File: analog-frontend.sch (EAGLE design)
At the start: 69 parts, among them IC1 TPS63031, IC2 ADG731, IC3 TM4C123G, IC4 INA332, IC5 NRF24L01SMD, IC6 OPA2320, Y1 CRYSTAL3X2, Y2 CRYSTAL3X2

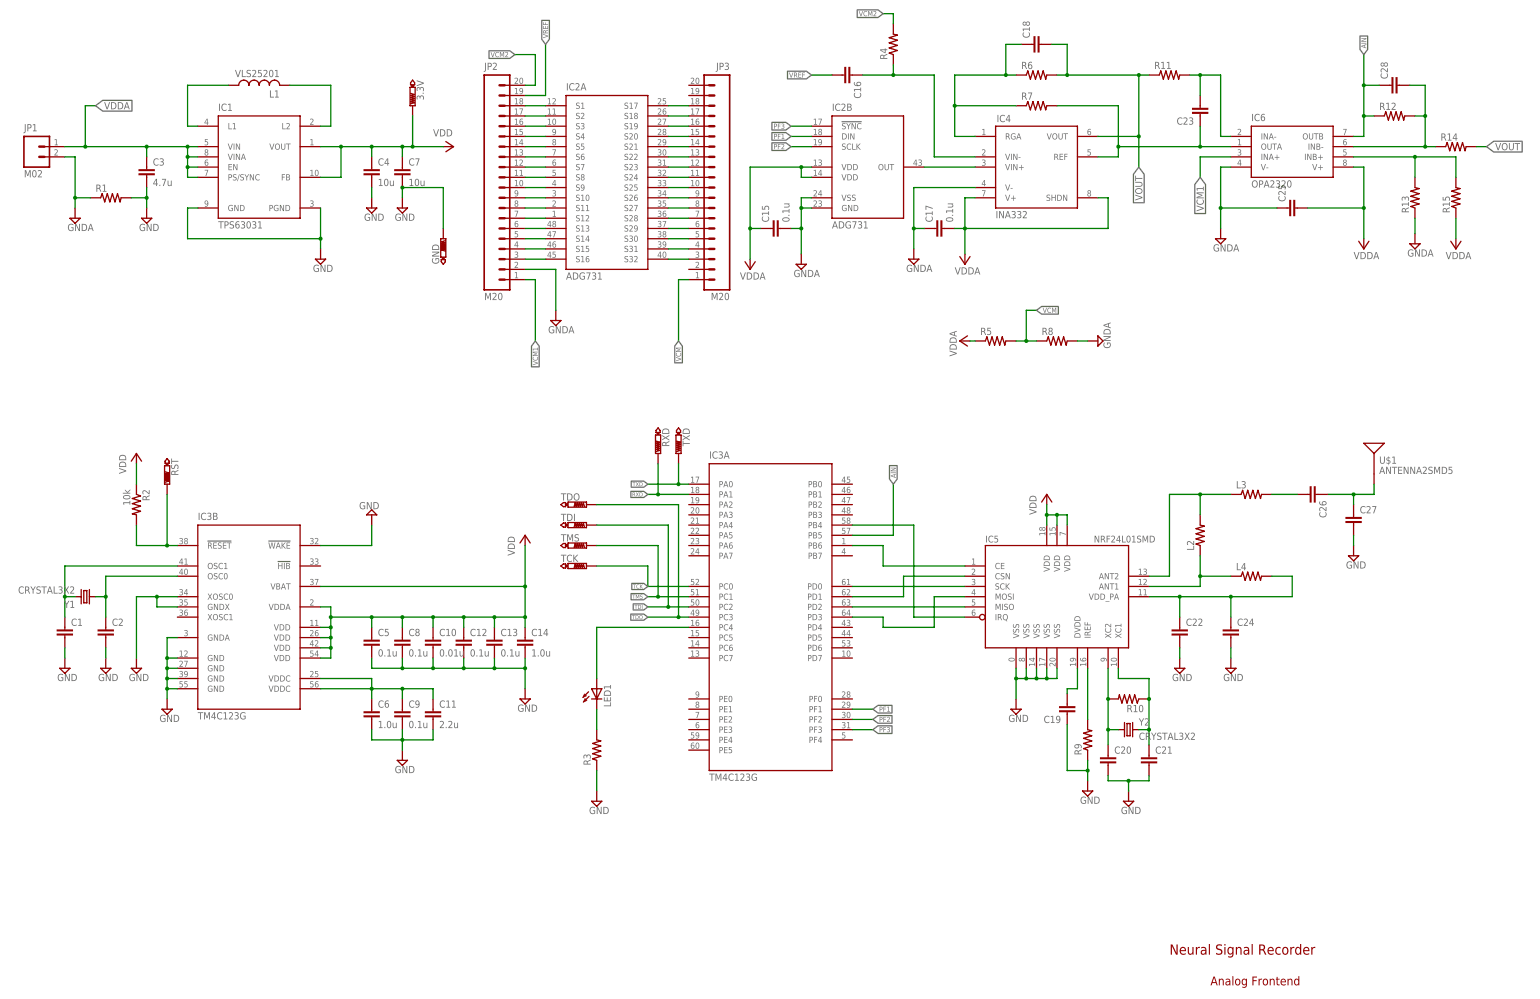
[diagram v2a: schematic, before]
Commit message: fixed component values
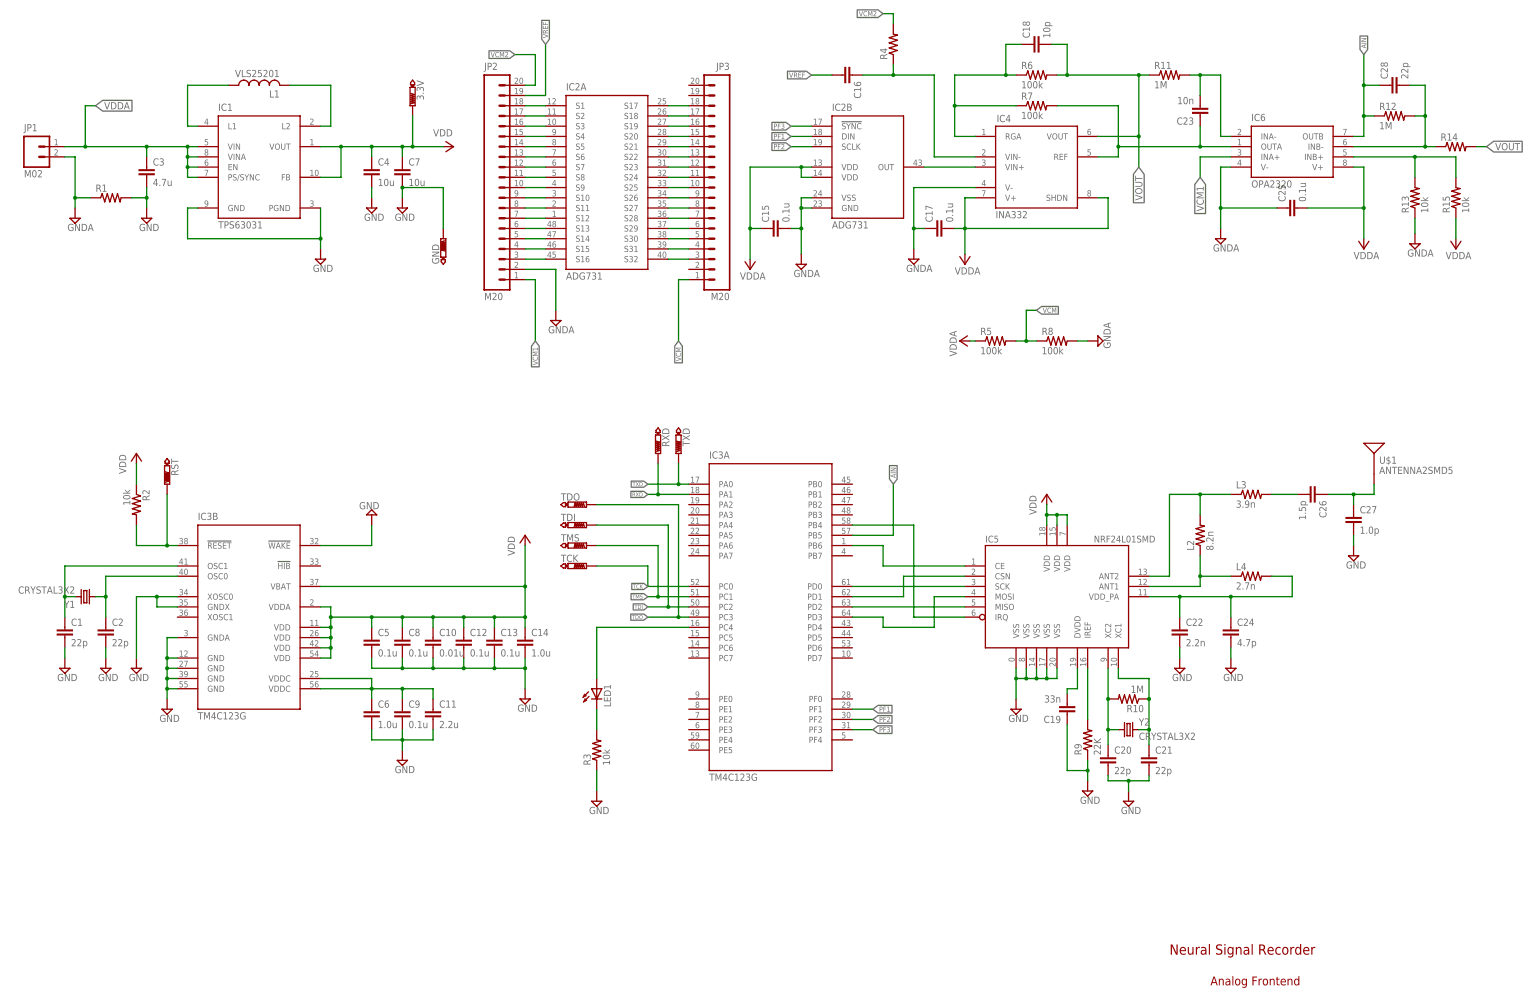
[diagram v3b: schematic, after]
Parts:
- C1, C2, C20, C21, C28: value (none) -> 22p
- C18: value (none) -> 10p
- C19: value (none) -> 33n
- C22: value (none) -> 2.2n
- C23: value (none) -> 10n
- C24: value (none) -> 4.7p
- C25: value (none) -> 0.1u
- C26: value (none) -> 1.5p
- C27: value (none) -> 1.0p
- L2: value (none) -> 8.2n
- L3: value (none) -> 3.9n
- L4: value (none) -> 2.7n
- R10, R11, R12: value (none) -> 1M
- R13, R15, R3: value (none) -> 10k
- R5, R6, R7, R8: value (none) -> 100k
- R9: value (none) -> 22K
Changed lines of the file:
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@@
 <part name="IC6" library="mor307" deviceset="OPA2320" device=""/>
 <part name="IC5" library="SparkFun-RF" deviceset="NRF24L01" device="SMD"/>
-<part name="R7" library="rcl" deviceset="R-US_" device="R0402"/>
-<part name="C18" library="rcl" deviceset="C-EU" device="C0402"/>
-<part name="R6" library="rcl" deviceset="R-US_" device="R0402"/>
-<part name="R11" library="rcl" deviceset="R-US_" device="R0402"/>
-<part name="C23" library="rcl" deviceset="C-EU" device="C0402"/>
+<part name="R7" library="rcl" deviceset="R-US_" device="R0402" value="100k"/>
+<part name="C18" library="rcl" deviceset="C-EU" device="C0402" value="10p"/>
+<part name="R6" library="rcl" deviceset="R-US_" device="R0402" value="100k"/>
+<part name="R11" library="rcl" deviceset="R-US_" device="R0402" value="1M"/>
+<part name="C23" library="rcl" deviceset="C-EU" device="C0402" value="10n"/>
 <part name="C17" library="rcl" deviceset="C-EU" device="C0402" value="0.1u"/>
 <part name="SUPPLY5" library="supply2" deviceset="GND" device="" value="GNDA"/>
-<part name="C25" library="rcl" deviceset="C-EU" device="C0402"/>
+<part name="C25" library="rcl" deviceset="C-EU" device="C0402" value="0.1u"/>
 <part name="SUPPLY6" library="supply2" deviceset="GND" device="" value="GNDA"/>
 <part name="R14" library="rcl" deviceset="R-US_" device="R0402"/>
-<part name="R12" library="rcl" deviceset="R-US_" device="R0402"/>
-<part name="C28" library="rcl" deviceset="C-EU" device="C0402"/>
-<part name="R13" library="rcl" deviceset="R-US_" device="R0402"/>
-<part name="R15" library="rcl" deviceset="R-US_" device="R0402"/>
+<part name="R12" library="rcl" deviceset="R-US_" device="R0402" value="1M"/>
+<part name="C28" library="rcl" deviceset="C-EU" device="C0402" value="22p"/>
+<part name="R13" library="rcl" deviceset="R-US_" device="R0402" value="10k"/>
+<part name="R15" library="rcl" deviceset="R-US_" device="R0402" value="10k"/>
 <part name="SUPPLY7" library="supply2" deviceset="GND" device="" value="GNDA"/>
 <part name="+3V1" library="supply1" deviceset="+3V3" device="" value="VDDA"/>
@@
 <part name="+3V5" library="supply1" deviceset="+3V3" device="" value="VDD"/>
 <part name="SUPPLY10" library="supply2" deviceset="GND" device=""/>
-<part name="C19" library="rcl" deviceset="C-EU" device="C0402"/>
-<part name="R9" library="rcl" deviceset="R-US_" device="R0402"/>
+<part name="C19" library="rcl" deviceset="C-EU" device="C0402" value="33n"/>
+<part name="R9" library="rcl" deviceset="R-US_" device="R0402" value="22K"/>
 <part name="SUPPLY12" library="supply2" deviceset="GND" device=""/>
 <part name="Y2" library="mor307" deviceset="CRYSTAL3X2" device=""/>
-<part name="C20" library="rcl" deviceset="C-EU" device="C0402"/>
-<part name="C21" library="rcl" deviceset="C-EU" device="C0402"/>
-<part name="R10" library="rcl" deviceset="R-US_" device="R0402"/>
+<part name="C20" library="rcl" deviceset="C-EU" device="C0402" value="22p"/>
+<part name="C21" library="rcl" deviceset="C-EU" device="C0402" value="22p"/>
+<part name="R10" library="rcl" deviceset="R-US_" device="R0402" value="1M"/>
 <part name="SUPPLY13" library="supply2" deviceset="GND" device=""/>
-<part name="L3" library="rcl" deviceset="R-US_" device="R0402"/>
-<part name="L4" library="rcl" deviceset="R-US_" device="R0402"/>
-<part name="L2" library="rcl" deviceset="R-US_" device="R0402"/>
-<part name="C26" library="rcl" deviceset="C-EU" device="C0402"/>
-<part name="C27" library="rcl" deviceset="C-EU" device="C0402"/>
-<part name="C22" library="rcl" deviceset="C-EU" device="C0402"/>
-<part name="C24" library="rcl" deviceset="C-EU" device="C0402"/>
+<part name="L3" library="rcl" deviceset="R-US_" device="R0402" value="3.9n"/>
+<part name="L4" library="rcl" deviceset="R-US_" device="R0402" value="2.7n"/>
+<part name="L2" library="rcl" deviceset="R-US_" device="R0402" value="8.2n"/>
+<part name="C26" library="rcl" deviceset="C-EU" device="C0402" value="1.5p"/>
+<part name="C27" library="rcl" deviceset="C-EU" device="C0402" value="1.0p"/>
+<part name="C22" library="rcl" deviceset="C-EU" device="C0402" value="2.2n"/>
+<part name="C24" library="rcl" deviceset="C-EU" device="C0402" value="4.7p"/>
 <part name="U$1" library="SparkFun-RF" deviceset="ANTENNA2" device="SMD5"/>
 <part name="SUPPLY14" library="supply2" deviceset="GND" device=""/>
@@
 <part name="+3V6" library="supply1" deviceset="+3V3" device="" value="VDD"/>
 <part name="Y1" library="mor307" deviceset="CRYSTAL3X2" device=""/>
-<part name="C1" library="rcl" deviceset="C-EU" device="C0402"/>
-<part name="C2" library="rcl" deviceset="C-EU" device="C0402"/>
+<part name="C1" library="rcl" deviceset="C-EU" device="C0402" value="22p"/>
+<part name="C2" library="rcl" deviceset="C-EU" device="C0402" value="22p"/>
 <part name="SUPPLY17" library="supply2" deviceset="GND" device=""/>
 <part name="SUPPLY18" library="supply2" deviceset="GND" device=""/>
@@
 <part name="+3V8" library="supply1" deviceset="+3V3" device="" value="VDD"/>
 <part name="SUPPLY23" library="supply2" deviceset="GND" device=""/>
-<part name="R5" library="rcl" deviceset="R-US_" device="R0402"/>
-<part name="R8" library="rcl" deviceset="R-US_" device="R0402"/>
+<part name="R5" library="rcl" deviceset="R-US_" device="R0402" value="100k"/>
+<part name="R8" library="rcl" deviceset="R-US_" device="R0402" value="100k"/>
 <part name="+3V9" library="supply1" deviceset="+3V3" device="" value="VDDA"/>
 <part name="SUPPLY24" library="supply2" deviceset="GND" device="" value="GNDA"/>
@@
 <part name="SUPPLY11" library="supply2" deviceset="GND" device="" value="GNDA"/>
 <part name="LED1" library="ng" deviceset="LED" device="0402"/>
-<part name="R3" library="rcl" deviceset="R-US_" device="R0402"/>
+<part name="R3" library="rcl" deviceset="R-US_" device="R0402" value="10k"/>
 <part name="SUPPLY25" library="supply2" deviceset="GND" device=""/>
 </parts>
